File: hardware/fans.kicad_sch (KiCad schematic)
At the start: 8 parts, among them Q5 PMV450ENEA

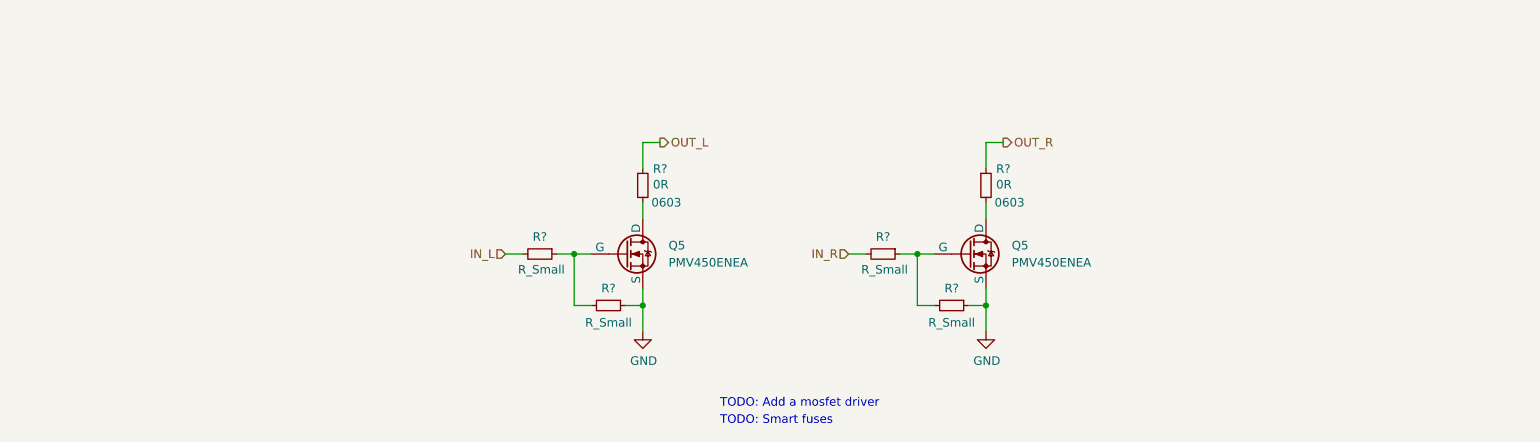
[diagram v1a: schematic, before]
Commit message: Improve the schematic
- add anti-aliasing filters
- rearrange the main connector signals
- improve the power filtering
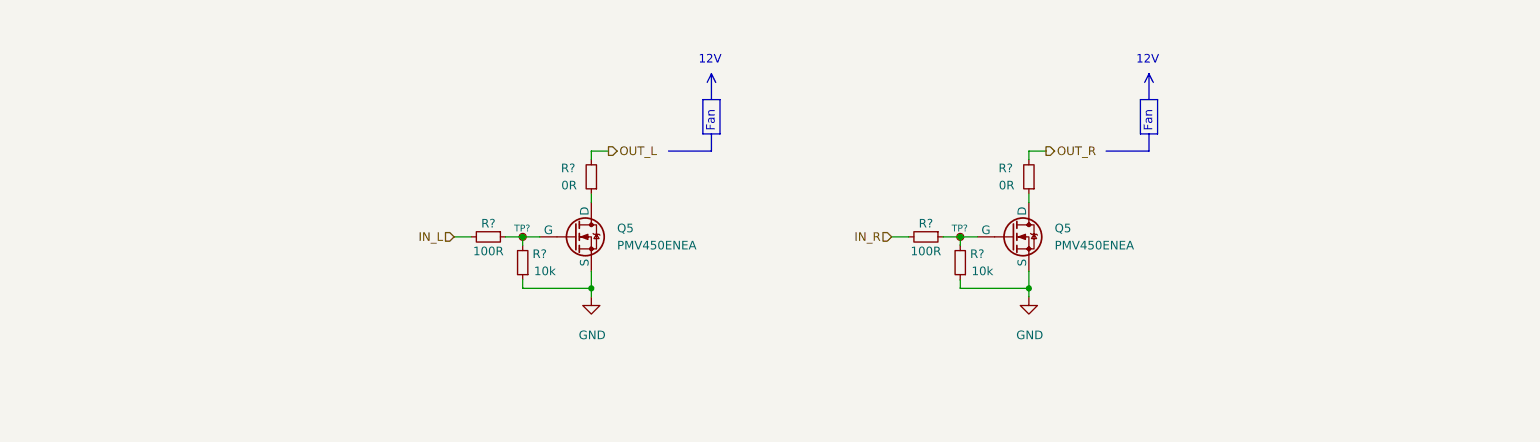
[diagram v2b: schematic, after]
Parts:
- removed Q5 (x2): PMV450ENEA, symbol Simulation_SPICE:NMOS
- removed R? (x4): R_Small, Resistor_SMD:R_0402_1005Metric, symbol Device:R_Small
- removed R? (x2): 0R, Resistor_SMD:R_0603_1608Metric, symbol Device:R_Small
- added Q5 (x2): PMV450ENEA, symbol Simulation_SPICE:NMOS
- added R? (x2): 0R, Resistor_SMD:R_0603_1608Metric, symbol Device:R_Small
- added R? (x2): 100R, Resistor_SMD:R_0603_1608Metric, symbol Device:R_Small
- added R? (x2): 10k, Resistor_SMD:R_0603_1608Metric, symbol Device:R_Small
- added TP? (x2): TestPoint_Small, TestPoint:TestPoint_Pad_D1.0mm, symbol Connector:TestPoint_Small
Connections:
- net GND: now also Q5.3 (S), Q5.3 (S), R?.1, R?.1
- net IN_L: now also R?.2
- net IN_R: now also R?.2
- net OUT_L: now also R?.2
- net OUT_R: now also R?.2
- new net: Q5.1 (D), R?.1 (x2)
- new net: Q5.2 (G), R?.1, R?.2, TP?.1 (x2)
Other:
- note added: "12V"
- note added: "Fan"
- note removed: "TODO: Add a mosfet driver"
- note removed: "TODO: Smart fuses"

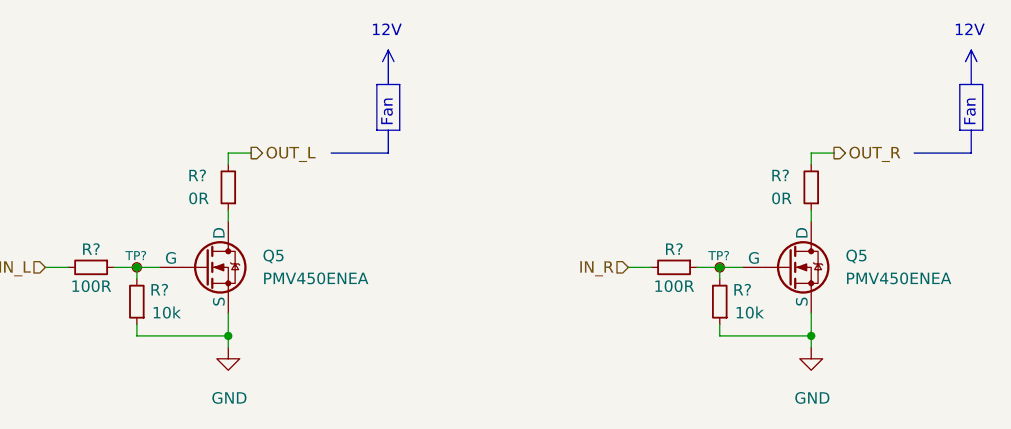
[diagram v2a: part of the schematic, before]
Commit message: Set component values
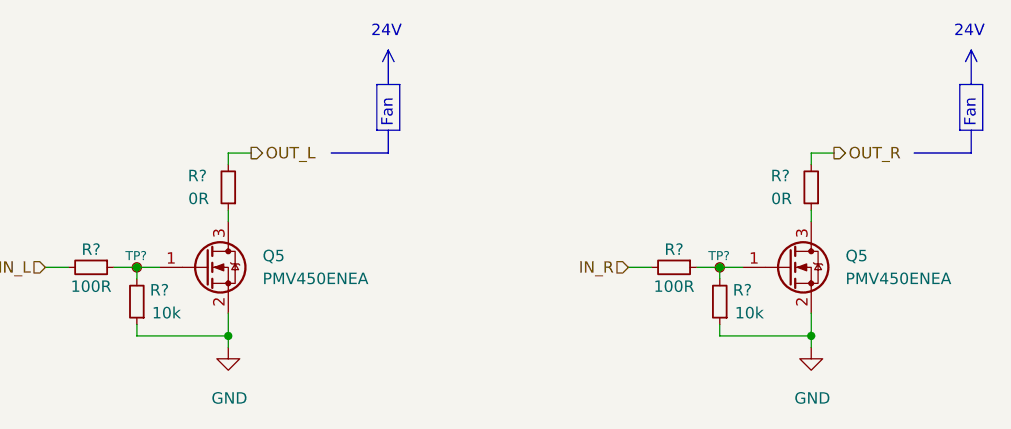
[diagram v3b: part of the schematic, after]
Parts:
- Q5: symbol Simulation_SPICE:NMOS -> Device:Q_NMOS_GSD
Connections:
- net GND: now also Q5.2 (S), Q5.2 (S); no longer Q5.3 (S), Q5.3 (S)
- net at R?.1: now also Q5.3 (D); no longer Q5.1 (D) (x2)
- net at R?.1, R?.2, TP?.1: now also Q5.1 (G); no longer Q5.2 (G) (x2)
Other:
- note added: "24V"
- note removed: "12V"
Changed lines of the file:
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@@
     (effects (font (size 1.27 1.27)) (justify left bottom))
   )
-  (text "12V" (at 201.295 76.2 0)
+  (text "24V" (at 201.295 76.2 0)
     (effects (font (size 1.27 1.27)) (justify left bottom))
   )
-  (text "12V" (at 136.525 76.2 0)
+  (text "24V" (at 136.525 76.2 0)
     (effects (font (size 1.27 1.27)) (justify left bottom))
   )
@@
         )
         (path "/b652b05a-4e3d-4ad1-b032-18886abe7d45/12f12a63-cabc-40cf-a64b-d1bd8b3dd459"
-          (reference "R46") (unit 1)
+          (reference "R48") (unit 1)
         )
         (path "/b652b05a-4e3d-4ad1-b032-18886abe7d45/2f82735d-d185-44cc-bb86-fc399780134d"
@@
     )
   )
-  (symbol (lib_id "Simulation_SPICE:NMOS") (at 118.11 101.6 0) (unit 1)
+  (symbol (lib_id "Device:Q_NMOS_GSD") (at 118.11 101.6 0) (unit 1)
     (in_bom yes) (on_board yes) (dnp no)
     (property "Reference" "Q5" (at 124.46 100.33 0)
@@
       (effects (font (size 1.27 1.27)) hide)
     )
-    (property "Datasheet" "https://assets.nexperia.com/documents/data-sheet/PMV450ENEA.pdf" (at 118.11 114.3 0)
+    (property "Datasheet" "~" (at 118.11 101.6 0)
       (effects (font (size 1.27 1.27)) hide)
     )
@@
         )
         (path "/b652b05a-4e3d-4ad1-b032-18886abe7d45/12f12a63-cabc-40cf-a64b-d1bd8b3dd459"
-          (reference "R44") (unit 1)
+          (reference "R46") (unit 1)
         )
       )
@@
         )
         (path "/b652b05a-4e3d-4ad1-b032-18886abe7d45/12f12a63-cabc-40cf-a64b-d1bd8b3dd459"
-          (reference "R45") (unit 1)
+          (reference "R47") (unit 1)
         )
       )
@@
         )
         (path "/b652b05a-4e3d-4ad1-b032-18886abe7d45/12f12a63-cabc-40cf-a64b-d1bd8b3dd459"
-          (reference "R48") (unit 1)
+          (reference "R50") (unit 1)
         )
       )
@@
     )
   )
-  (symbol (lib_id "Simulation_SPICE:NMOS") (at 182.88 101.6 0) (unit 1)
+  (symbol (lib_id "Device:Q_NMOS_GSD") (at 182.88 101.6 0) (unit 1)
     (in_bom yes) (on_board yes) (dnp no)
     (property "Reference" "Q5" (at 189.23 100.33 0)
@@
       (effects (font (size 1.27 1.27)) hide)
     )
-    (property "Datasheet" "https://assets.nexperia.com/documents/data-sheet/PMV450ENEA.pdf" (at 182.88 114.3 0)
+    (property "Datasheet" "~" (at 182.88 101.6 0)
       (effects (font (size 1.27 1.27)) hide)
     )
@@
         )
         (path "/b652b05a-4e3d-4ad1-b032-18886abe7d45/12f12a63-cabc-40cf-a64b-d1bd8b3dd459"
-          (reference "R49") (unit 1)
+          (reference "R51") (unit 1)
         )
         (path "/b652b05a-4e3d-4ad1-b032-18886abe7d45/2f82735d-d185-44cc-bb86-fc399780134d"
@@
         )
         (path "/b652b05a-4e3d-4ad1-b032-18886abe7d45/12f12a63-cabc-40cf-a64b-d1bd8b3dd459"
-          (reference "R47") (unit 1)
-        )
-      )
+          (reference "R49") (unit 1)
+        )
+      )

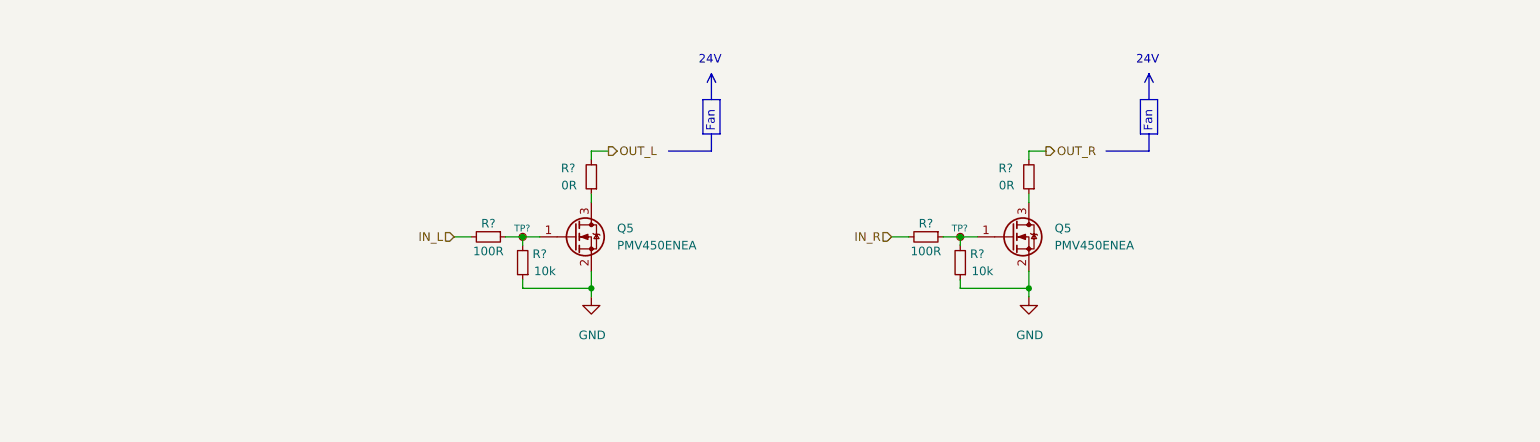
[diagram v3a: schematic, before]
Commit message: Improve the schematic according to the feedback
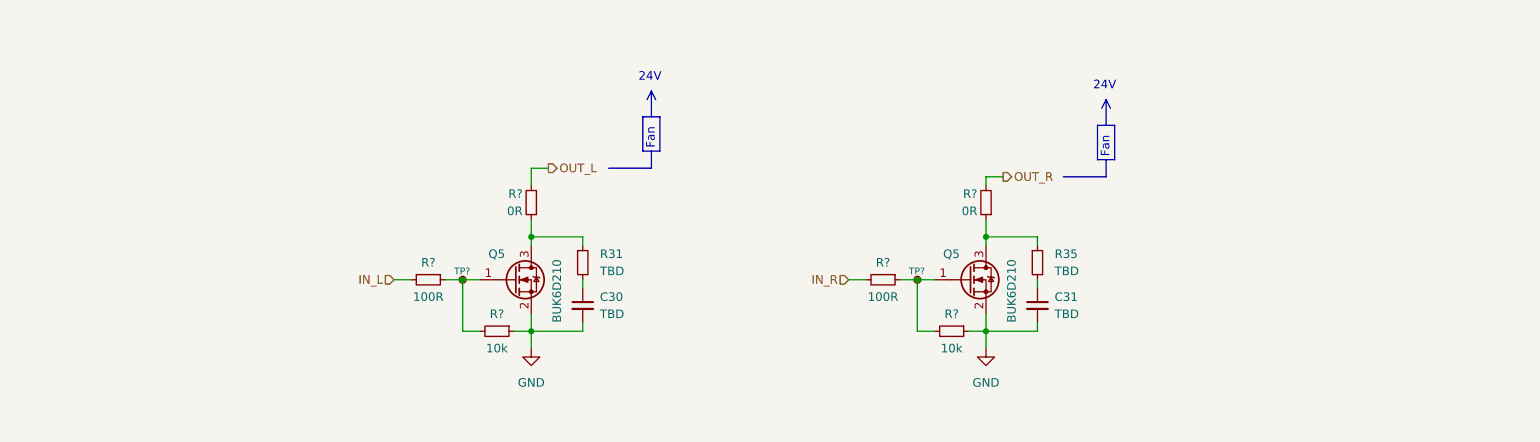
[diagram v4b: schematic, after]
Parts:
- removed Q5 (x2): PMV450ENEA, symbol Device:Q_NMOS_GSD
- removed R? (x2): 0R, Resistor_SMD:R_0603_1608Metric, symbol Device:R_Small
- removed R? (x2): 100R, Resistor_SMD:R_0603_1608Metric, symbol Device:R_Small
- removed R? (x2): 10k, Resistor_SMD:R_0603_1608Metric, symbol Device:R_Small
- removed TP? (x2): TestPoint_Small, TestPoint:TestPoint_Pad_D1.0mm, symbol Connector:TestPoint_Small
- added C30, C31: TBD, Capacitor_SMD:C_0603_1608Metric, symbol Device:C_Small
- added Q5 (x2): BUK6D210, Package_DFN_QFN:Diodes_UDFN2020-6_Type-F, symbol Device:Q_NMOS_GSD
- added R31, R35: TBD, Resistor_SMD:R_0603_1608Metric, symbol Device:R_Small
- added R? (x2): 10k, Resistor_SMD:R_0603_1608Metric, symbol Device:R_Small
- added R? (x2): 100R, Resistor_SMD:R_0603_1608Metric, symbol Device:R_Small
- added R? (x2): 0R, Resistor_SMD:R_0603_1608Metric, symbol Device:R_Small
- added TP? (x2): TestPoint_Small, TestPoint:TestPoint_Pad_D1.0mm, symbol Connector:TestPoint_Small
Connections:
- net GND: now also C30.2, C31.2, Q5.2 (S), Q5.2 (S), R?.1, R?.1
- net IN_L: now also R?.2
- net IN_R: now also R?.2
- net OUT_L: now also R?.2
- net OUT_R: now also R?.2
- new net: Q5.1 (G), R?.1, R?.2, TP?.1 (x2)
- new net: Q5.3 (D), R35.1, R?.1
- new net: C31.1, R35.2
- new net: C30.1, R31.2
- new net: Q5.3 (D), R31.1, R?.1

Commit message: Add high-side drivers to the fans and pumps
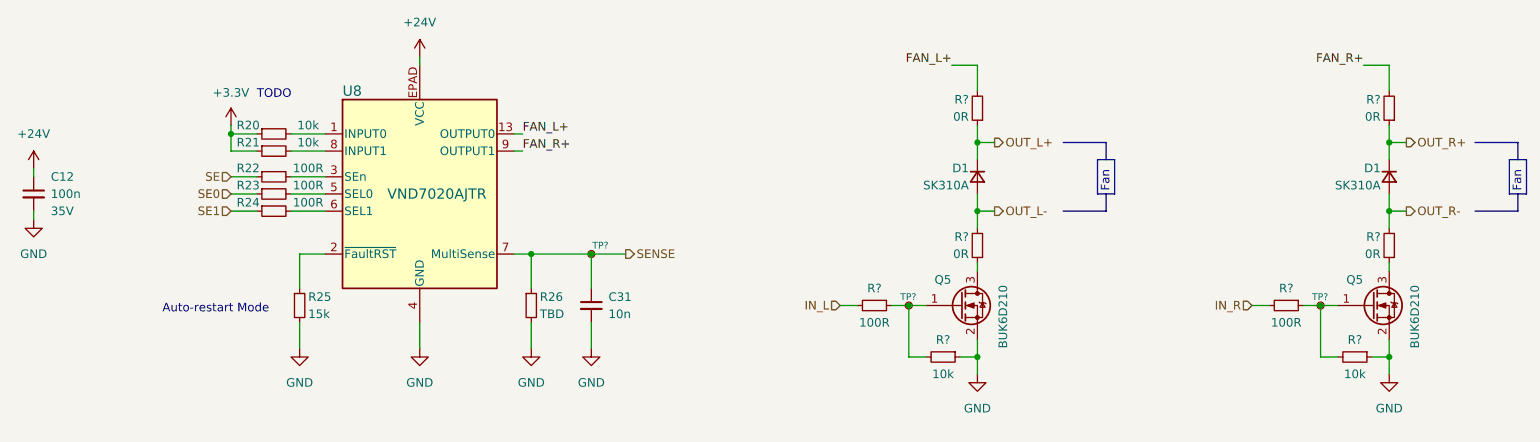
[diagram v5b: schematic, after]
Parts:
- removed C30: TBD, Capacitor_SMD:C_0603_1608Metric, symbol Device:C_Small
- removed R31, R35: TBD, Resistor_SMD:R_0603_1608Metric, symbol Device:R_Small
- removed R?: 0R, Resistor_SMD:R_0603_1608Metric, symbol Device:R_Small
- added C12: 100n, Capacitor_SMD:C_0603_1608Metric, symbol Device:C_Small
- added D1 (x2): SK310A, Diode_SMD:D_SMA, symbol Device:D_Small
- added R20, R21: 10k, symbol Device:R_Small
- added R22, R23, R24: 100R, symbol Device:R_Small
- added R25: 15k, symbol Device:R_Small
- added R26: TBD, symbol Device:R_Small
- added R? (x3): 0R, Resistor_SMD:R_0603_1608Metric, symbol Device:R_Small
- added TP?: TestPoint_Small, TestPoint:TestPoint_Pad_D1.0mm, symbol Connector:TestPoint_Small
- added U8: VND7020AJTR, Local_Library:VND7020AJTR, symbol VND7020AJTR:VND7020AJTR
- C31: value TBD -> 10n; footprint Capacitor_SMD:C_0603_1608Metric -> (none)
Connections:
- net GND: now also C12.2, R25.2, R26.2, U8.4 (GND)
- net at Q5.3 (D): now also R?.1
- net SENSE: now reaches C31.1
- net SENSE: now also R26.1, TP?.1, U8.7 (MultiSense)
- net OUT_L renamed OUT_L-
- net OUT_L-: now also D1.2 (A)
- new net: R20.2, U8.1 (INPUT0)
- new net: R25.1, U8.2 (~{FaultRST})
- new net: R22.2, U8.3 (SEn)
- new net: R23.2, U8.5 (SEL0)
- new net: R24.2, U8.6 (SEL1)
- new net: R21.2, U8.8 (INPUT1)
- new net +24V: C12.1, U8.EPAD (VCC)
- new net +3.3V: R20.1, R21.1
- new net FAN_L+: R?.2, U8.13 (OUTPUT0), U8.14 (OUTPUT0), U8.15 (OUTPUT0), U8.16 (OUTPUT0)
- new net FAN_R+: R?.2, U8.10 (OUTPUT1), U8.11 (OUTPUT1), U8.12 (OUTPUT1), U8.9 (OUTPUT1)
- new net OUT_L+: D1.1 (K), R?.1
- new net OUT_R+: D1.1 (K), R?.1
- new net OUT_R-: D1.2 (A), R?.2
- new net SE: R22.1
- new net SE0: R23.1
- new net SE1: R24.1
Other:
- note added: "Auto-restart Mode"
- note added: "TODO"
- note removed: "24V"
- moved on the sheet: Q5, R?, TP?

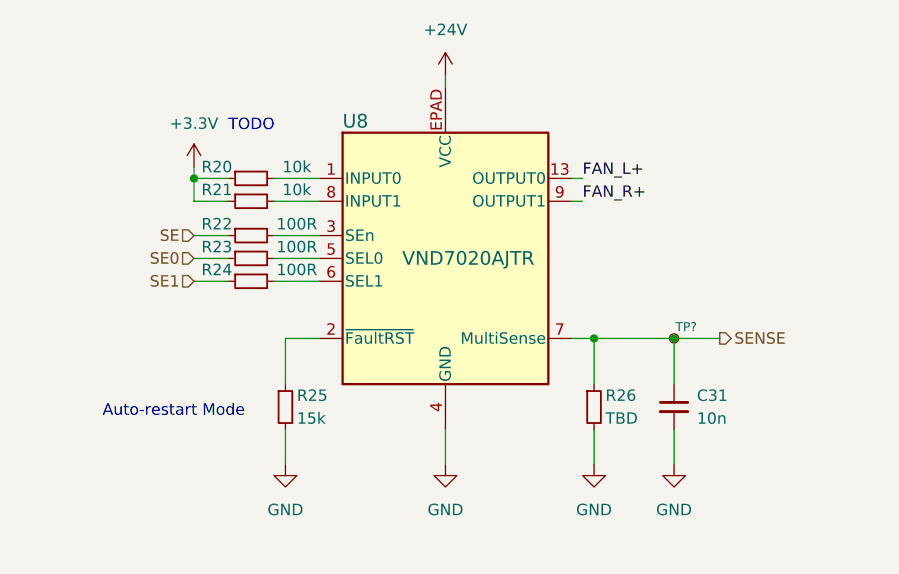
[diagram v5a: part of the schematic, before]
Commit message: Improve the diagram based on the feedback
- add an input LC filter
- remove the USB connector
- add a programmer connector
- move optocouplers into a subsheet
- add a suspension tension meter IC
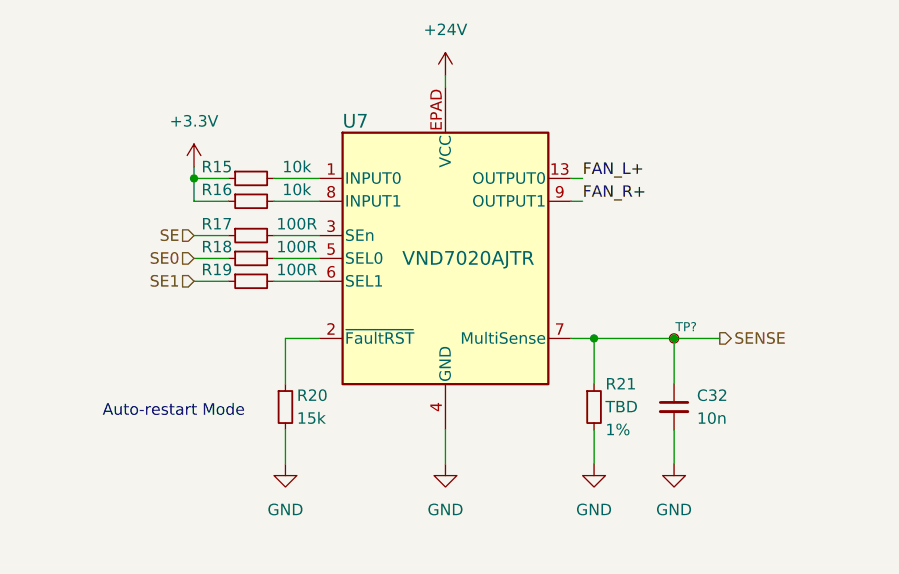
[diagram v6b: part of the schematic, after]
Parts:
- C12: Rated Voltage (none) -> 35V; Voltage 35V -> (none)
- C32: renamed from C31; footprint (none) -> Capacitor_SMD:C_0603_1608Metric
- R15: renamed from R20; footprint (none) -> Resistor_SMD:R_0603_1608Metric
- R16: renamed from R21; footprint (none) -> Resistor_SMD:R_0603_1608Metric
- R17: renamed from R22; footprint (none) -> Resistor_SMD:R_0603_1608Metric
- R18: renamed from R23; footprint (none) -> Resistor_SMD:R_0603_1608Metric
- R19: renamed from R24; footprint (none) -> Resistor_SMD:R_0603_1608Metric
- R20: renamed from R25; footprint (none) -> Resistor_SMD:R_0603_1608Metric
- R21: renamed from R26; footprint (none) -> Resistor_SMD:R_0603_1608Metric; Tolerance (none) -> 1%
- renumbered U8 to U7
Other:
- note removed: "TODO"
